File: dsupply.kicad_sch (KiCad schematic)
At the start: 66 parts, among them J8 Barrel_Jack, Q3 BC857, Q4 AOSP21321, Q5 AOSP21321, Q6 BC857, Q7 BC857, Q8 AOSP21321, Q9 BC857, U22 PM1202, U23 TPS54620, U24 AMS1117-3.3

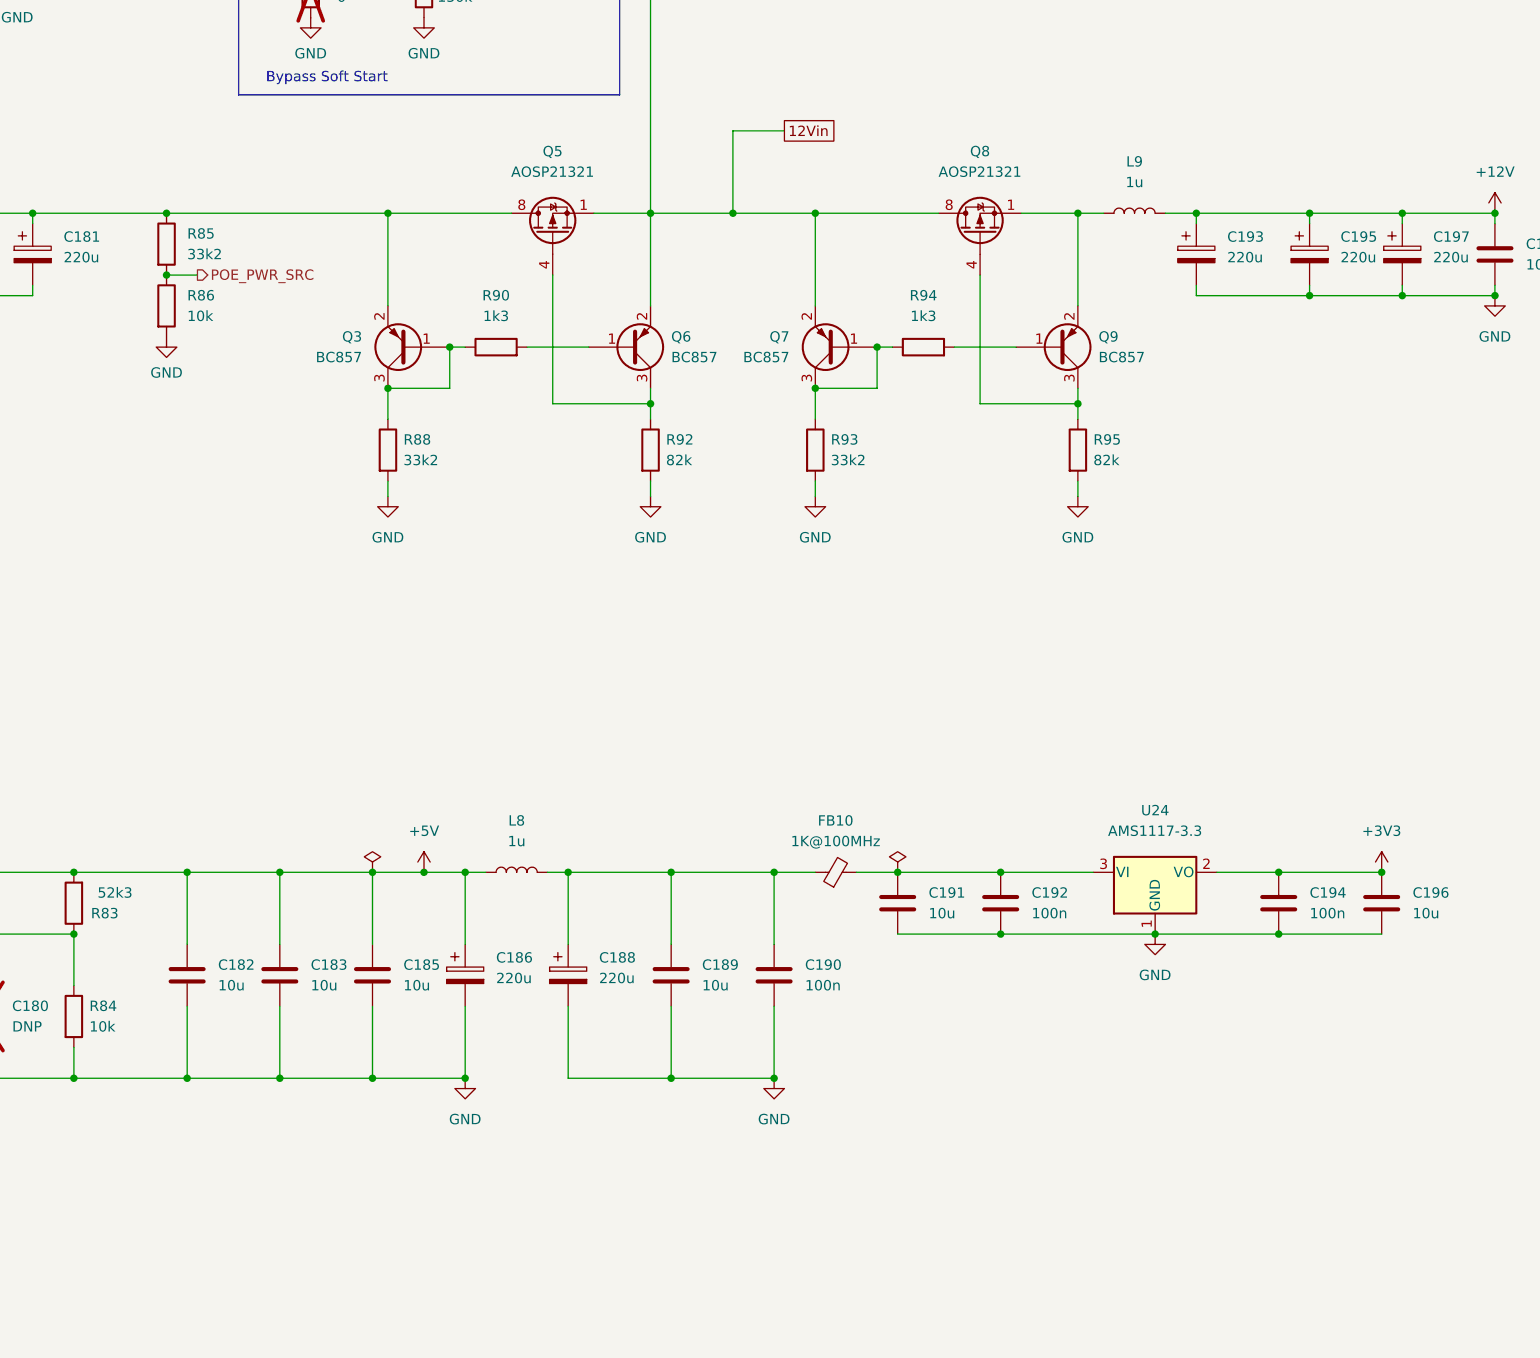
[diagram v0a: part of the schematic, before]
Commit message: sch, pcb: Add LEDs and TPs to Critical Power Rails
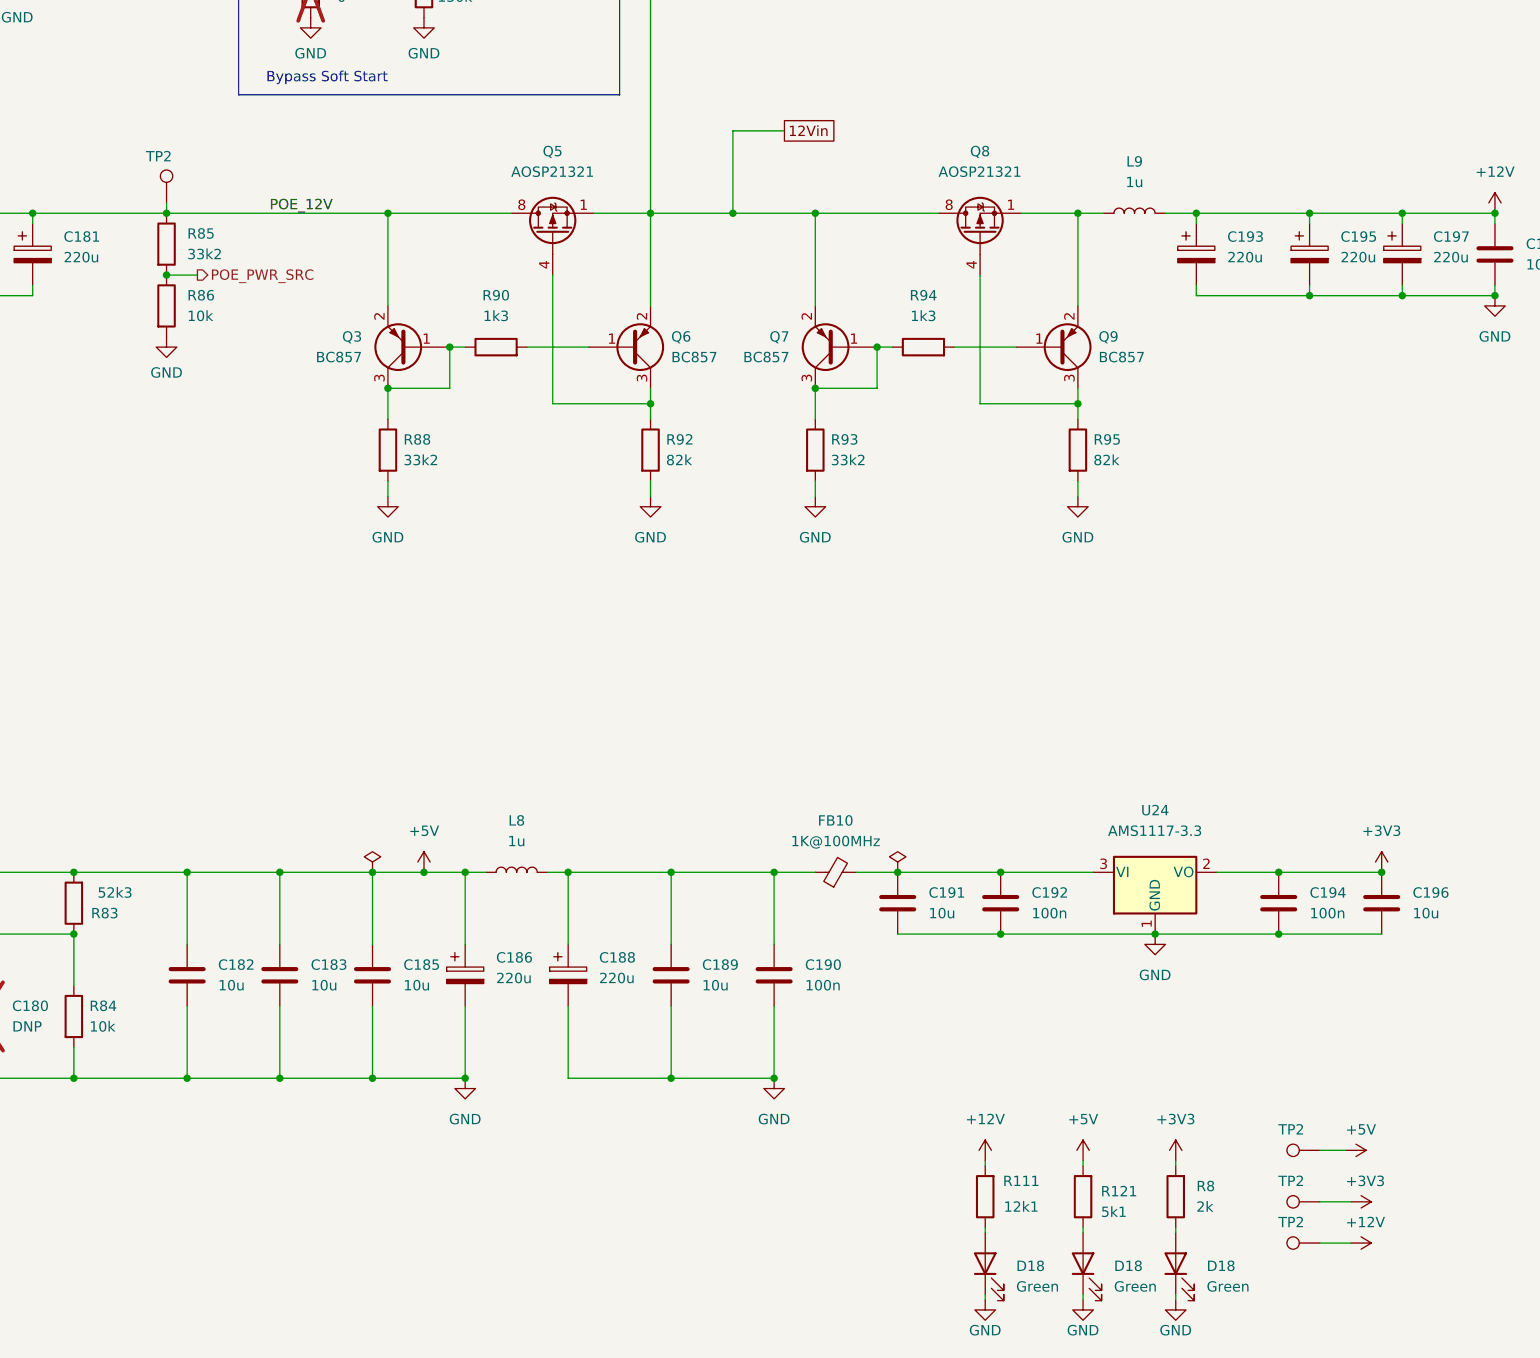
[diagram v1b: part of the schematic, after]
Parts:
- added D18 (x3): Green, LED_SMD:LED_0603_1608Metric, symbol Device:LED
- added R111: 12k1, Resistor_SMD:R_0603_1608Metric, symbol Device:R
- added R121: 5k1, Resistor_SMD:R_0603_1608Metric, symbol Device:R
- added R8: 2k, Resistor_SMD:R_0603_1608Metric, symbol Device:R
- added TP2 (x4): TestPoint, TestPoint:TestPoint_Pad_1.0x1.0mm, symbol Connector:TestPoint
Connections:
- net +12V: now also R111.2, TP2.1
- net +3V3: now also R8.2, TP2.1
- net +5V: now also R121.2, TP2.1
- net GND: now also D18.1 (K), D18.1 (K), D18.1 (K)
- net POE_12V: now reaches C181.1, L6.2, Q3.2 (E), Q5.5 (D), Q5.6 (D), Q5.7 (D), Q5.8 (D), R85.1
- net POE_12V: now also TP2.1
- new net: D18.2 (A), R111.1
- new net: D18.2 (A), R121.1
- new net: D18.2 (A), R8.1

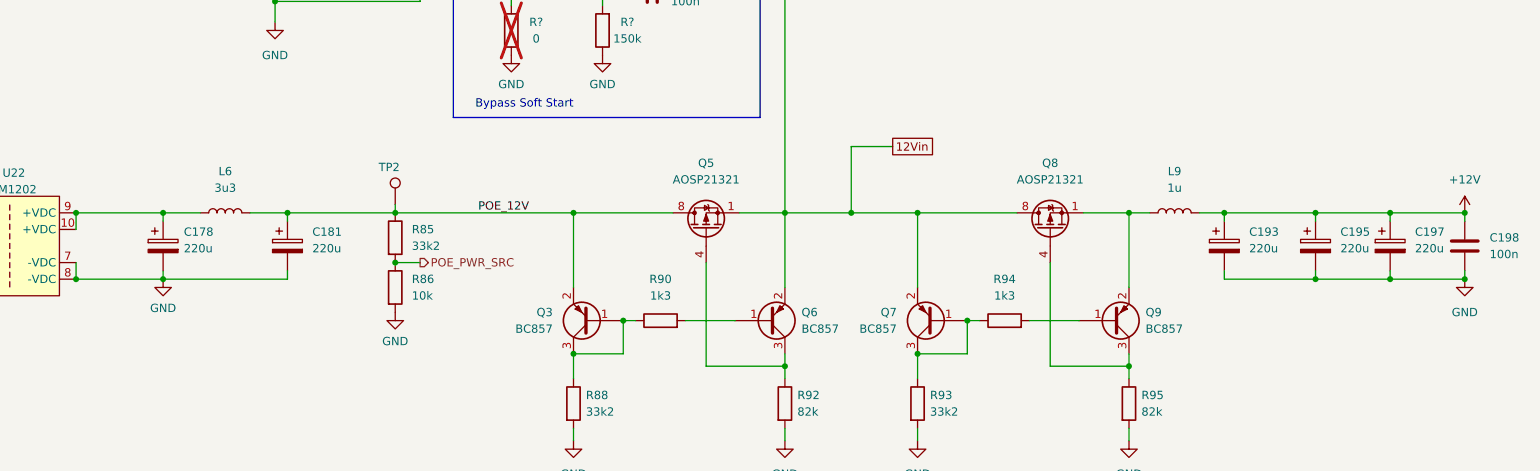
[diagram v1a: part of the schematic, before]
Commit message: sch, pcb: Remove X7R, X5R at input LT304x - Reduce the number of Tantalum Capacitor Used - Replace some non critical ones with Electrolytic Caps
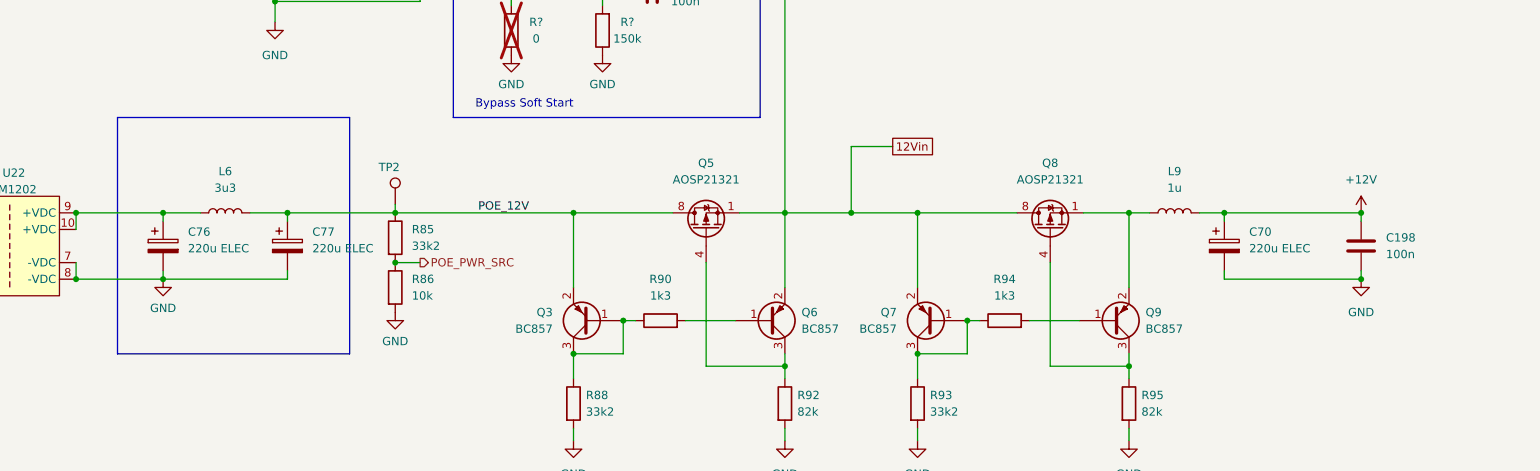
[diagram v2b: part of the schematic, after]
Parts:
- removed C178, C181, C193, C195, C197: 220u, Capacitor_Tantalum_SMD:CP_EIA-7343-15_Kemet-W, symbol Device:C_Polarized
- added C70, C76, C77: 220u ELEC, kirdy:Cap_Elec_SMD_865080345012, symbol Device:C_Polarized
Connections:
- net +12V: now also C70.1
- net GND: now also C70.2, C76.2, C77.2
- net POE_12V: now also C77.1
- net at L6.1, U22.10 (+VDC), U22.9 (+VDC): now also C76.1
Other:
- moved on the sheet: C198

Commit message: Cleanup and Update Modification Date
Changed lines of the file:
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@@
   (title_block
     (title "digital supply")
-    (date "2023-11-09")
+    (date "2023-11-27")
     (rev "r0_3")
     (company "M-Labs Limited")
@@
     (stroke (width 0) (type default))
   )
-  (rectangle (start 172.085 61.595) (end 207.645 97.79)
-    (stroke (width 0) (type default))
-    (fill (type none))
-  )
   (rectangle (start 223.52 14.605) (end 270.51 61.595)

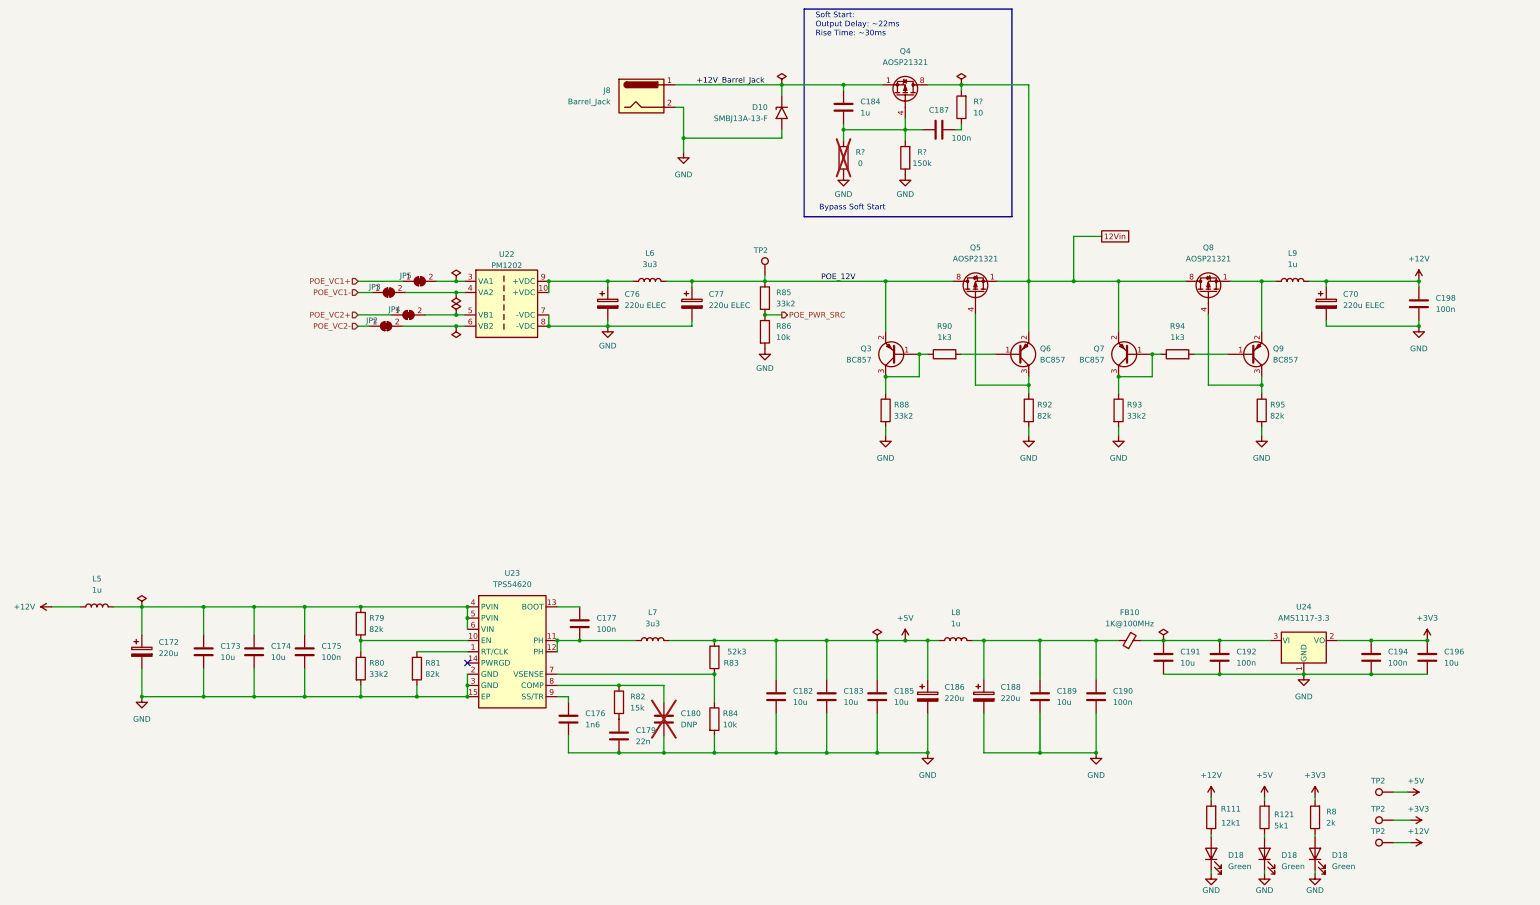
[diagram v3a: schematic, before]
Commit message: Reassign Reference Designators for all Symbols
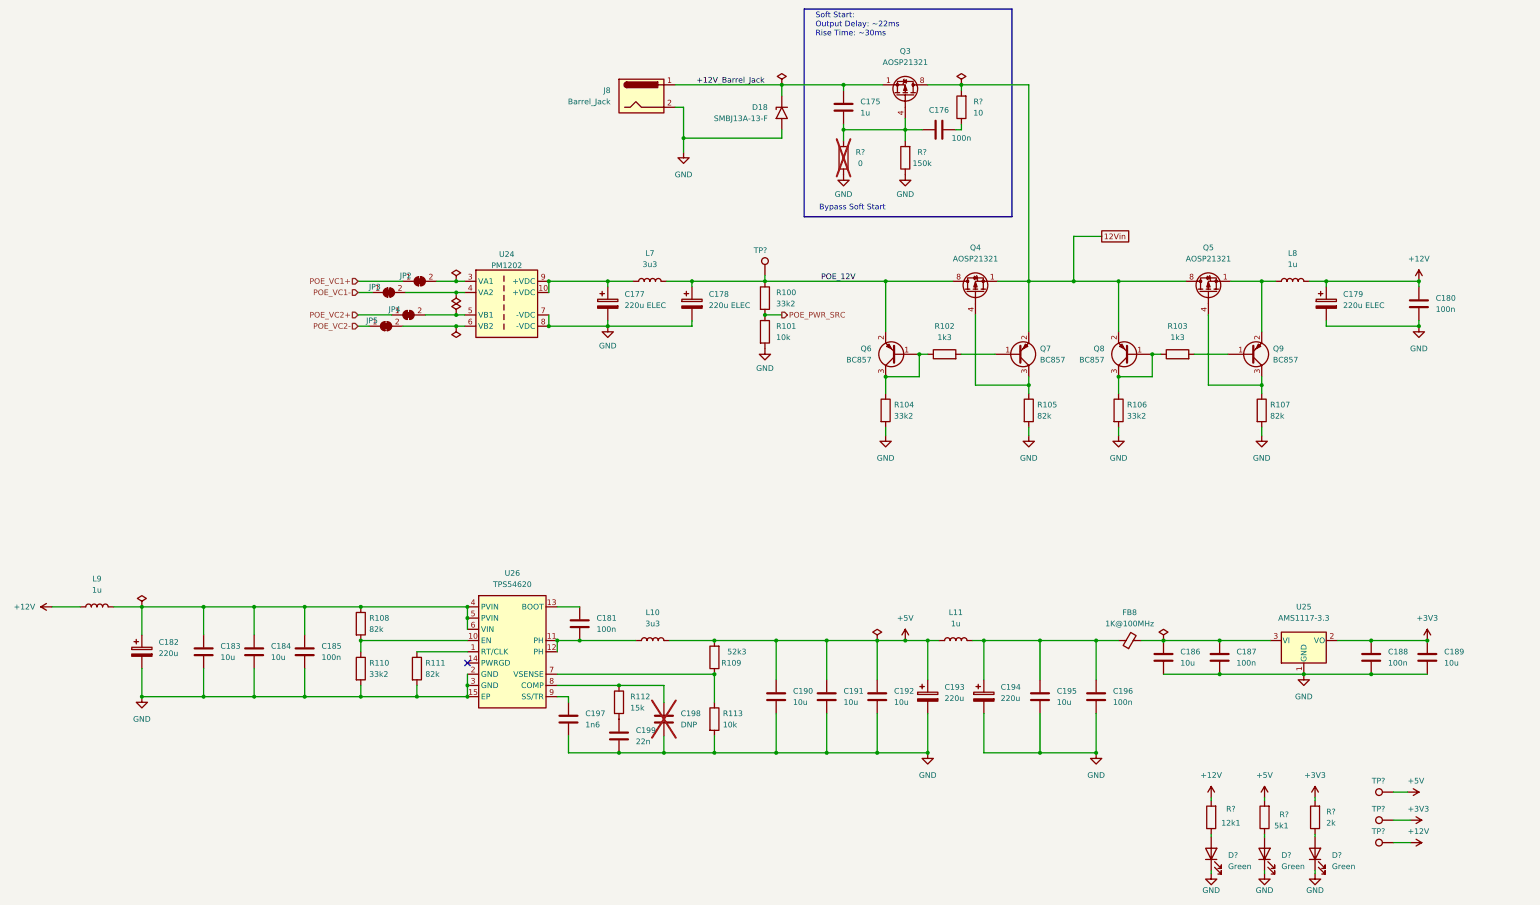
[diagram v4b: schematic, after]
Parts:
- renumbered C184 to C175, C187 to C176, C76 to C177, C77 to C178, C70 to C179, C198 to C180, C177 to C181, C172 to C182, C173 to C183, C174 to C184, C175 to C185, C191 to C186, C192 to C187, C194 to C188, C196 to C189, C182 to C190, C183 to C191, C185 to C192, C186 to C193, C188 to C194, C189 to C195, C190 to C196, C176 to C197, C180 to C198, C179 to C199, D10 to D18, D18 to D?, FB10 to FB8, JP5 to JP2, JP2 to JP5, L7 to L10, L8 to L11, L6 to L7, L9 to L8, L5 to L9, Q4 to Q3, Q5 to Q4, Q8 to Q5, Q3 to Q6, Q6 to Q7, Q7 to Q8, R85 to R100, R86 to R101, R90 to R102, R94 to R103, R88 to R104, R92 to R105, R93 to R106, R95 to R107, R79 to R108, R83 to R109, R80 to R110, R81 to R111, R82 to R112, R84 to R113, R121 to R?, R8 to R?, R111 to R?, TP2 to TP?, U22 to U24, U24 to U25, U23 to U26
